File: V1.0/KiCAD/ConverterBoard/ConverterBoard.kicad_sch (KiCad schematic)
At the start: 10 parts

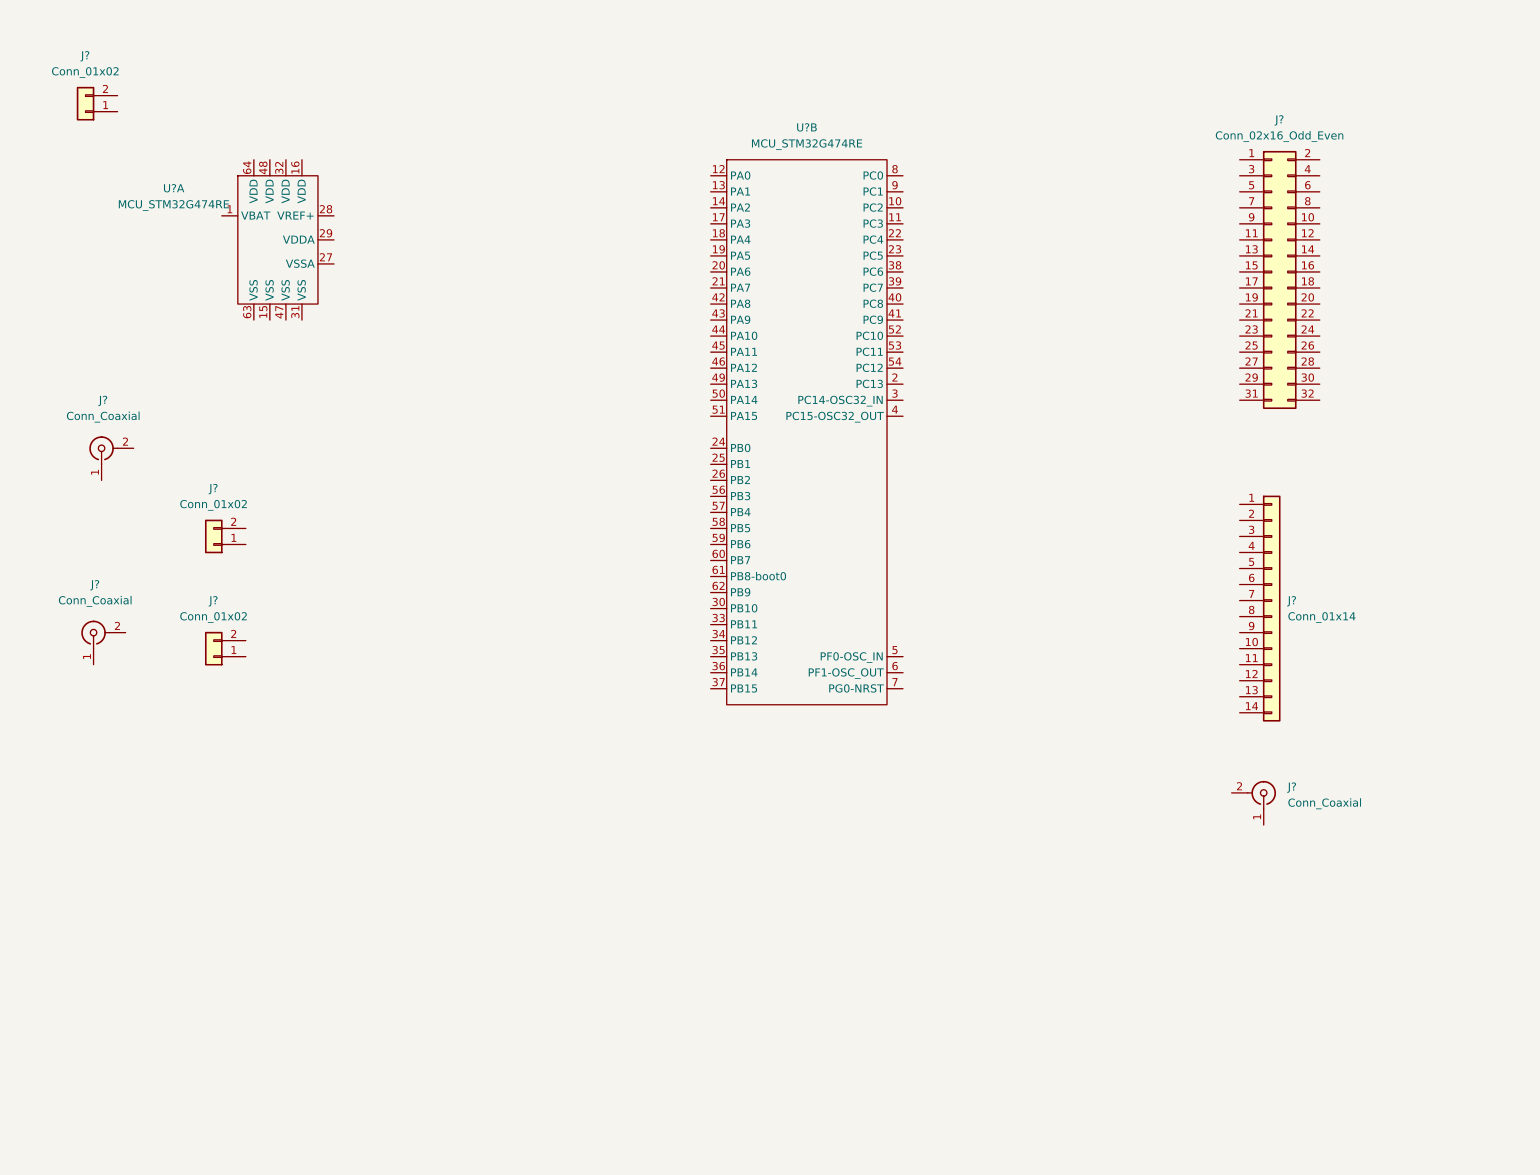
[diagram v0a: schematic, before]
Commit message: README update and PCB outputs
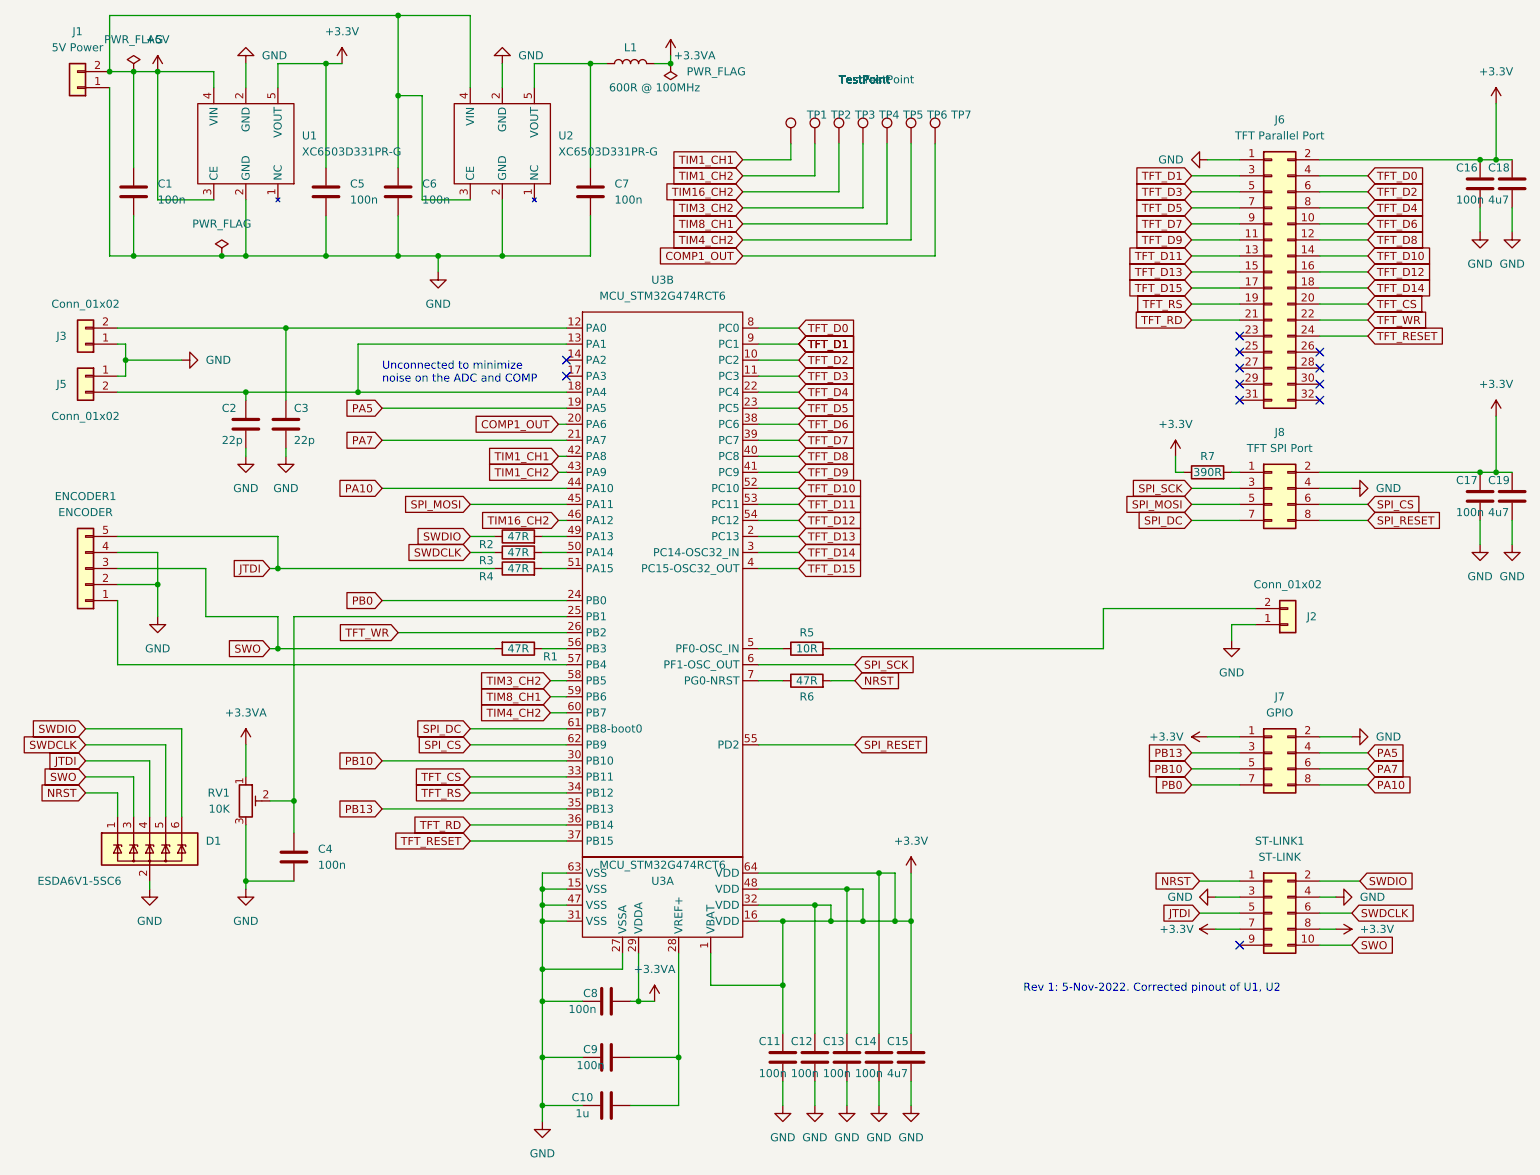
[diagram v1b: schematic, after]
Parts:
- removed J?: Conn_01x14, symbol Connector_Generic:Conn_01x14
- removed J? (x3): Conn_Coaxial, symbol Connector:Conn_Coaxial
- added C1, C11, C12, C13, C14, C16, C17, C4, C5, C6, C7, C8, C9: 100n, Capacitor_SMD:C_0805_2012Metric, symbol Device:C
- added C10: 1u, Capacitor_SMD:C_0805_2012Metric, symbol Device:C
- added C15, C18, C19: 4u7, Capacitor_SMD:C_0805_2012Metric, symbol Device:C
- added C2, C3: 22p, Capacitor_SMD:C_0805_2012Metric, symbol Device:C
- added D1: ESDA6V1-5SC6, Package_TO_SOT_SMD:SOT-23-6, symbol Power_Protection:ESDA6V1-5SC6
- added ENCODER1: ENCODER, Connector_PinHeader_2.54mm:PinHeader_1x05_P2.54mm_Vertical, symbol Connector_Generic:Conn_01x05
- added J2: Conn_01x02, Connector_PinHeader_2.54mm:PinHeader_1x02_P2.54mm_Vertical, symbol Connector_Generic:Conn_01x02
- added J7: GPIO, Connector_PinHeader_2.54mm:PinHeader_2x04_P2.54mm_Vertical, symbol Connector_Generic:Conn_02x04_Odd_Even
- added J8: TFT SPI Port, Connector_PinHeader_2.54mm:PinHeader_2x04_P2.54mm_Vertical, symbol Connector_Generic:Conn_02x04_Odd_Even
- added L1: 600R @ 100MHz, Inductor_SMD:L_0805_2012Metric_Pad1.15x1.40mm_HandSolder, symbol Device:L
- added R1, R2, R3, R4, R6: 47R, Resistor_SMD:R_0805_2012Metric_Pad1.20x1.40mm_HandSolder, symbol Device:R
- added R5: 10R, Resistor_SMD:R_0805_2012Metric_Pad1.20x1.40mm_HandSolder, symbol Device:R
- added R7: 390R, Resistor_SMD:R_0805_2012Metric_Pad1.20x1.40mm_HandSolder, symbol Device:R
- added RV1: 10K, Potentiometer_THT:Potentiometer_Bourns_3005_Horizontal, symbol Device:R_Potentiometer_Trim
- added ST-LINK1: ST-LINK, Connector_PinHeader_2.54mm:PinHeader_2x05_P2.54mm_Vertical, symbol Connector_Generic:Conn_02x05_Odd_Even
- added TP1, TP2, TP3, TP4, TP5, TP6, TP7: TestPoint, TestPoint:TestPoint_THTPad_1.5x1.5mm_Drill0.7mm, symbol Connector:TestPoint
- added U1, U2: XC6503D331PR-G, Package_TO_SOT_SMD:SOT-89-5_Handsoldering, symbol UKMaker:XC6503D331PR-G
- J1: renamed from J?; value Conn_01x02 -> 5V Power; footprint (none) -> TerminalBlock:TerminalBlock_bornier-2_P5.08mm
- J3, J5: renamed from J?; footprint (none) -> Connector_PinHeader_2.54mm:PinHeader_1x02_P2.54mm_Vertical
- J6: renamed from J?; value Conn_02x16_Odd_Even -> TFT Parallel Port; footprint (none) -> Connector_PinHeader_2.54mm:PinHeader_2x16_P2.54mm_Vertical
- U3: renamed from U?; value MCU_STM32G474RE -> MCU_STM32G474RCT6; footprint (none) -> Package_QFP:LQFP-64_10x10mm_P0.5mm
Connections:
- net TFT_D2: now reaches U3.10 (PC2)
- net TFT_D2: now also J6.6 (Pin_6)
- net TFT_D3: now reaches U3.11 (PC3)
- net TFT_D3: now also J6.5 (Pin_5)
- net at U3.12 (PA0): now also J3.2 (Pin_2), C3.1
- net at U3.13 (PA1): now also J5.2 (Pin_2), U3.18 (PA4), C2.1
- net PA5: now reaches U3.19 (PA5)
- net PA5: now also J7.4 (Pin_4)
- net TFT_D13: now reaches U3.2 (PC13)
- net TFT_D13: now also J6.15 (Pin_15)
- net COMP1_OUT: now reaches U3.20 (PA6)
- net COMP1_OUT: now also TP7.1
- net PA7: now reaches U3.21 (PA7)
- net PA7: now also J7.6 (Pin_6)
- net TFT_D4: now reaches U3.22 (PC4)
- net TFT_D4: now also J6.8 (Pin_8)
- net TFT_D5: now reaches U3.23 (PC5)
- net TFT_D5: now also J6.7 (Pin_7)
- net PB0: now reaches U3.24 (PB0)
- net PB0: now also J7.7 (Pin_7)
- net at U3.25 (PB1): now also C4.1, RV1.2
- net TFT_WR: now reaches U3.26 (PB2)
- net TFT_WR: now also J6.22 (Pin_22)
- net TFT_D14: now reaches U3.3 (PC14-OSC32_IN)
- net TFT_D14: now also J6.18 (Pin_18)
- net PB10: now reaches U3.30 (PB10)
- net PB10: now also J7.5 (Pin_5)
- net TFT_CS: now reaches U3.33 (PB11)
- net TFT_CS: now also J6.20 (Pin_20)
- net TFT_RS: now reaches U3.34 (PB12)
- net TFT_RS: now also J6.19 (Pin_19)
- net PB13: now reaches U3.35 (PB13)
- net PB13: now also J7.3 (Pin_3)
- net TFT_RD: now reaches U3.36 (PB14)
- net TFT_RD: now also J6.21 (Pin_21)
- net TFT_RESET: now reaches U3.37 (PB15)
- net TFT_RESET: now also J6.24 (Pin_24)
- net TFT_D6: now reaches U3.38 (PC6)
- net TFT_D6: now also J6.10 (Pin_10)
- net TFT_D7: now reaches U3.39 (PC7)
- net TFT_D7: now also J6.9 (Pin_9)
- net TFT_D15: now reaches U3.4 (PC15-OSC32_OUT)
- net TFT_D15: now also J6.17 (Pin_17)
- net TFT_D8: now reaches U3.40 (PC8)
- net TFT_D8: now also J6.12 (Pin_12)
- net TFT_D9: now reaches U3.41 (PC9)
- net TFT_D9: now also J6.11 (Pin_11)
- net TIM1_CH1: now reaches U3.42 (PA8)
- net TIM1_CH1: now also TP1.1
- net TIM1_CH2: now reaches U3.43 (PA9)
- net TIM1_CH2: now also TP2.1
- net PA10: now reaches U3.44 (PA10)
- net PA10: now also J7.8 (Pin_8)
- net SPI_MOSI: now reaches U3.45 (PA11)
- net SPI_MOSI: now also J8.5 (Pin_5)
- net TIM16_CH2: now reaches U3.46 (PA12)
- net TIM16_CH2: now also TP3.1
- net at U3.49 (PA13): now also R2.2
- net at U3.5 (PF0-OSC_IN): now also R5.1
- net at U3.50 (PA14): now also R3.2
- net at U3.51 (PA15): now also R4.2
- net TFT_D10: now reaches U3.52 (PC10)
- net TFT_D10: now also J6.14 (Pin_14)
- net TFT_D11: now reaches U3.53 (PC11)
- net TFT_D11: now also J6.13 (Pin_13)
- net TFT_D12: now reaches U3.54 (PC12)
- net TFT_D12: now also J6.16 (Pin_16)
- net at U3.56 (PB3): now also R1.1
- net at U3.57 (PB4): now also ENCODER1.1 (Pin_1)
- net TIM3_CH2: now reaches U3.58 (PB5)
- net TIM3_CH2: now also TP4.1
- net TIM8_CH1: now reaches U3.59 (PB6)
- net TIM8_CH1: now also TP5.1
- net SPI_SCK: now reaches U3.6 (PF1-OSC_OUT)
- net SPI_SCK: now also J8.3 (Pin_3)
- net TIM4_CH2: now reaches U3.60 (PB7)
- net TIM4_CH2: now also TP6.1
- net SPI_DC: now reaches U3.61 (PB8-boot0)
- net SPI_DC: now also J8.7 (Pin_7)
- net SPI_CS: now reaches U3.62 (PB9)
- net SPI_CS: now also J8.6 (Pin_6)
- net at U3.7 (PG0-NRST): now also R6.1
- net TFT_D0: now reaches U3.8 (PC0)
- net TFT_D0: now also J6.4 (Pin_4)
- net TFT_D1: now reaches U3.9 (PC1)
- net TFT_D1: now also J6.3 (Pin_3)
- net GND: now reaches J5.1 (Pin_1)
- net GND: now also J1.1 (Pin_1), J3.1 (Pin_1), J6.1 (Pin_1), U3.15 (VSS), U3.27 (VSSA), U3.31 (VSS), U3.47 (VSS), U3.63 (VSS), C1.2, C10.1, C11.2, C12.2, C13.2, C14.2, C15.2, C16.2, C17.2, C18.2, C19.2, C2.2, C3.2, C4.2, C5.2, C6.2, C7.2, C8.1, C9.1, D1.2 (GND), ENCODER1.2 (Pin_2), ENCODER1.4 (Pin_4), J2.1 (Pin_1), J7.2 (Pin_2), J8.4 (Pin_4), RV1.3, ST-LINK1.3 (Pin_3), ST-LINK1.4 (Pin_4), U1.2 (GND), U2.2 (GND)
- net +5V: now reaches J1.2 (Pin_2)
- net +5V: now also C1.1, C6.1, U1.3 (CE), U1.4 (VIN), U2.3 (CE), U2.4 (VIN)
- net +3.3V: now reaches J6.2 (Pin_2)
- net +3.3V: now also U3.1 (VBAT), U3.16 (VDD), U3.32 (VDD), U3.48 (VDD), U3.64 (VDD), C11.1, C12.1, C13.1, C14.1, C15.1, C16.1, C17.1, C18.1, C19.1, C5.1, J7.1 (Pin_1), J8.2 (Pin_2), R7.1, ST-LINK1.7 (Pin_7), ST-LINK1.8 (Pin_8), U1.5 (VOUT)
- net at U3.28 (VREF+): now also C10.2, C9.2
- net +3.3VA: now reaches U3.29 (VDDA)
- net +3.3VA: now also C8.2, L1.2, RV1.1
- new net: J2.2 (Pin_2), R5.2
- new net: J8.1 (Pin_1), R7.2
- new net: C7.1, L1.1, U2.5 (VOUT)
- new net JTDI: D1.4 (IO3), ENCODER1.5 (Pin_5), R4.1, ST-LINK1.5 (Pin_5)
- new net NRST: D1.1 (IO1), R6.2, ST-LINK1.1 (Pin_1)
- new net SPI_RESET: J8.8 (Pin_8), U3.55 (PD2)
- new net SWDCLK: D1.5 (IO4), R3.1, ST-LINK1.6 (Pin_6)
- new net SWDIO: D1.6 (IO5), R2.1, ST-LINK1.2 (Pin_2)
- new net SWO: D1.3 (IO2), ENCODER1.3 (Pin_3), R1.2, ST-LINK1.10 (Pin_10)
- no-connect marks 0 -> 12
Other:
- note added: "Rev 1: 5-Nov-2022. Corrected pinout of U1, U2"
- note added: "Unconnected to minimize noise on the ADC and COMP"
- moved on the sheet: J1, J3, J5, U3A
